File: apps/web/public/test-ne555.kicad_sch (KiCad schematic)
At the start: 9 parts, among them J1 PWR_5V, U1 NE555P

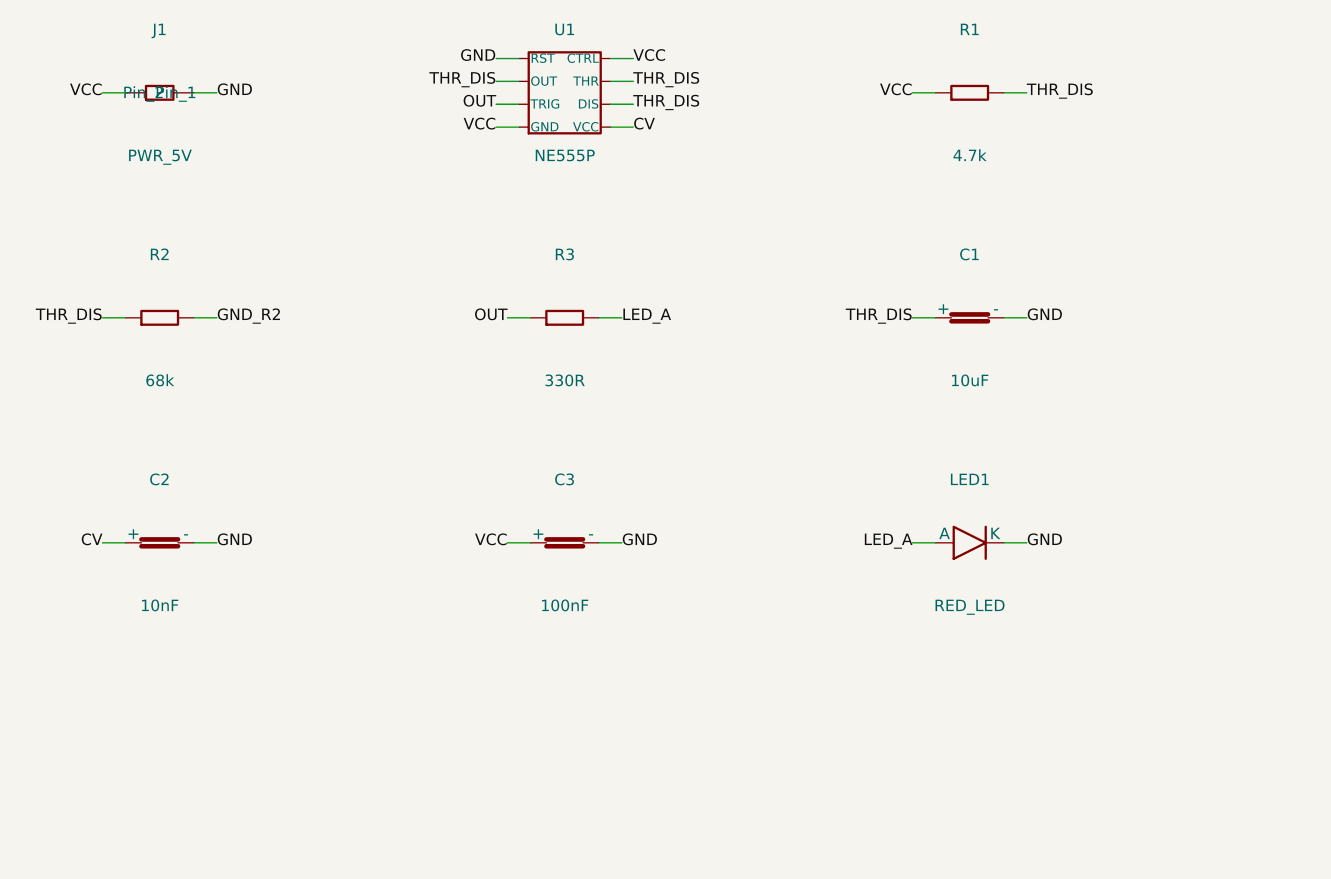
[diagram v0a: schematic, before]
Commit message: fix: increase schematic margins to keep components inside KiCanvas frame border
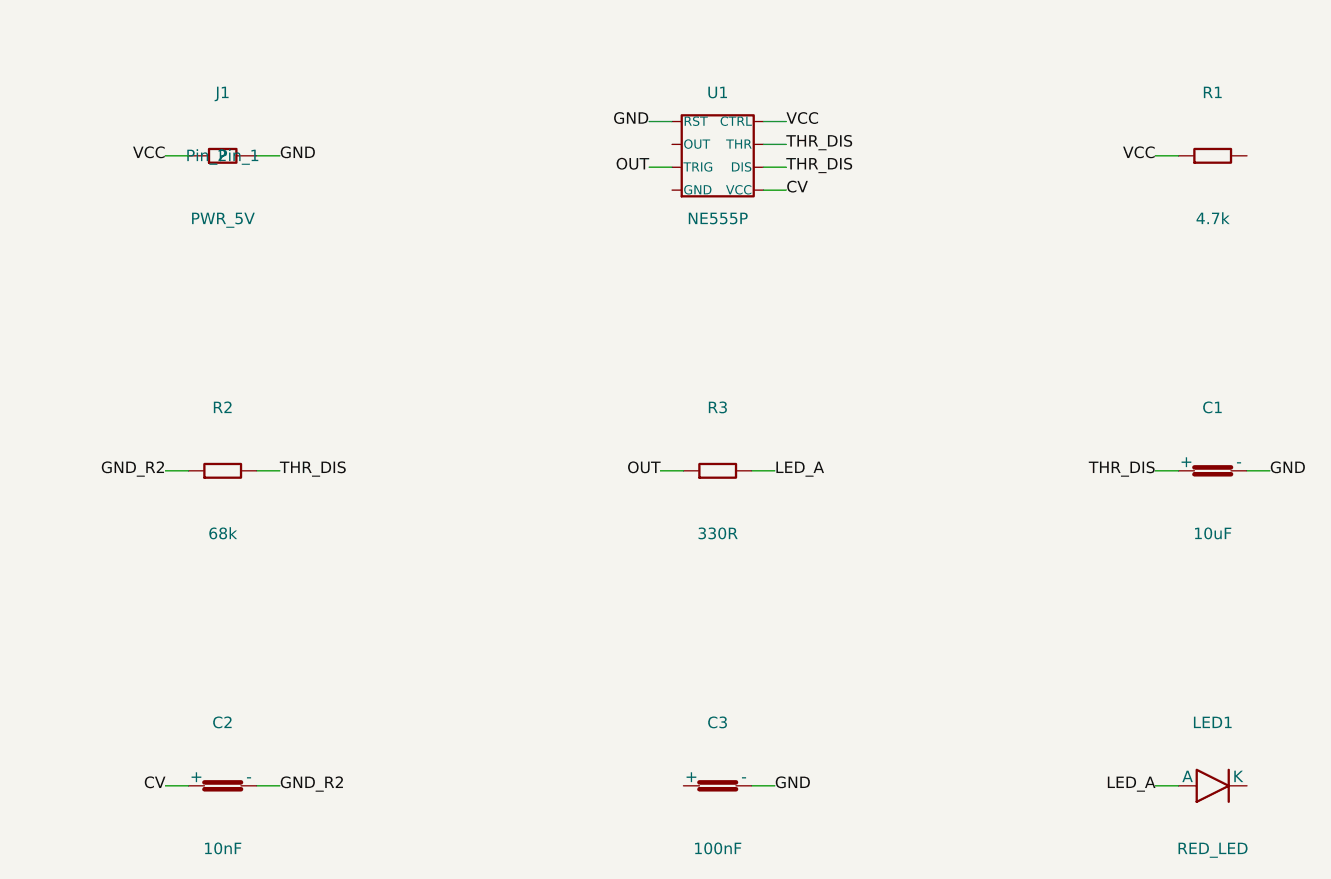
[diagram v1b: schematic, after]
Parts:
- C1: footprint Capacitor_SMD:C_1206_3216Metric -> Capacitor_THT:C_Radial_D5.0mm_H11.0mm_P2.00mm
- C2, C3: footprint Capacitor_SMD:C_0603_1608Metric -> Capacitor_THT:C_Disc_D5.0mm_W2.5mm_P5.00mm
- LED1: footprint LED_SMD:LED_0603_1608Metric -> LED_THT:LED_D5.0mm
- R1, R2, R3: footprint Resistor_SMD:R_0603_1608Metric -> Resistor_THT:R_Axial_DIN0207_L6.3mm_D2.5mm_P10.16mm_Horizontal
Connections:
- net GND: no longer C2.2 (-), LED1.2 (K)
- net GND_R2: now also C2.2 (-), R2.1; no longer R2.2
- net THR_DIS: now also R2.2; no longer R1.2, R2.1, U1.3 (OUT)
- net VCC: no longer C3.1 (+), U1.1 (GND)
